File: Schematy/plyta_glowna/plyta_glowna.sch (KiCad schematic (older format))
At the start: 6 parts

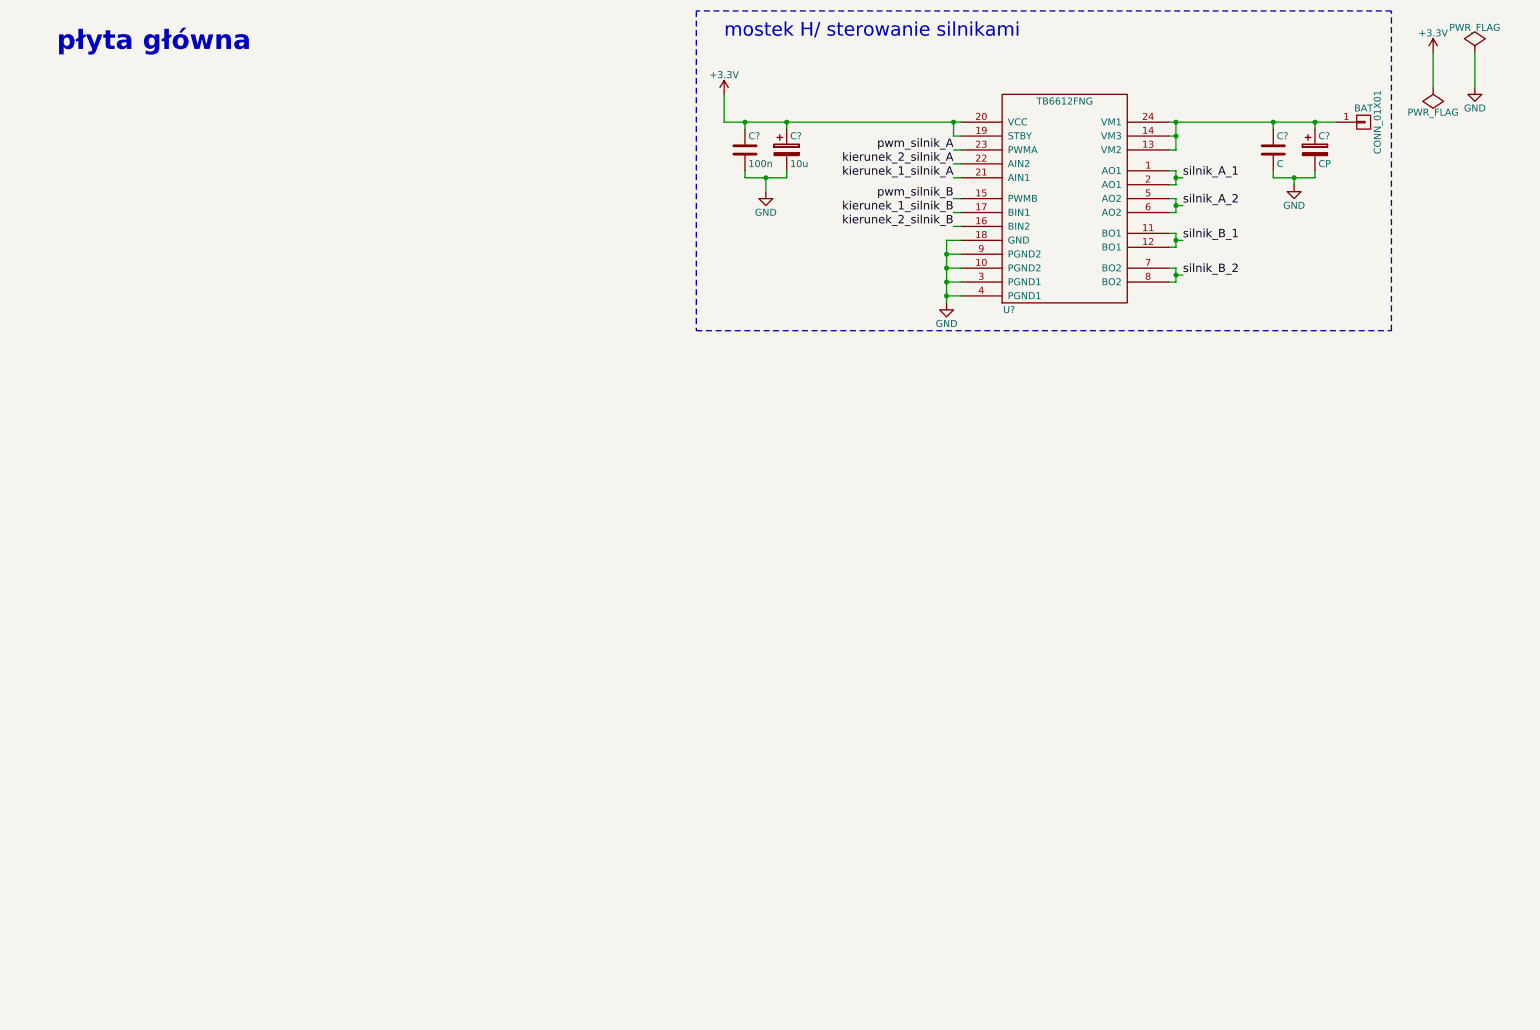
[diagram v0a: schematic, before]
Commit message: Płyta główna + listwa [do sprawdzenia]
do zrobienia:
- układ pomiarowy napięcia na akumulatorze
- wskaźnik naładowania akumulatora na 3 led
- dobrać złącza
- zagospodarować pozostałe piny
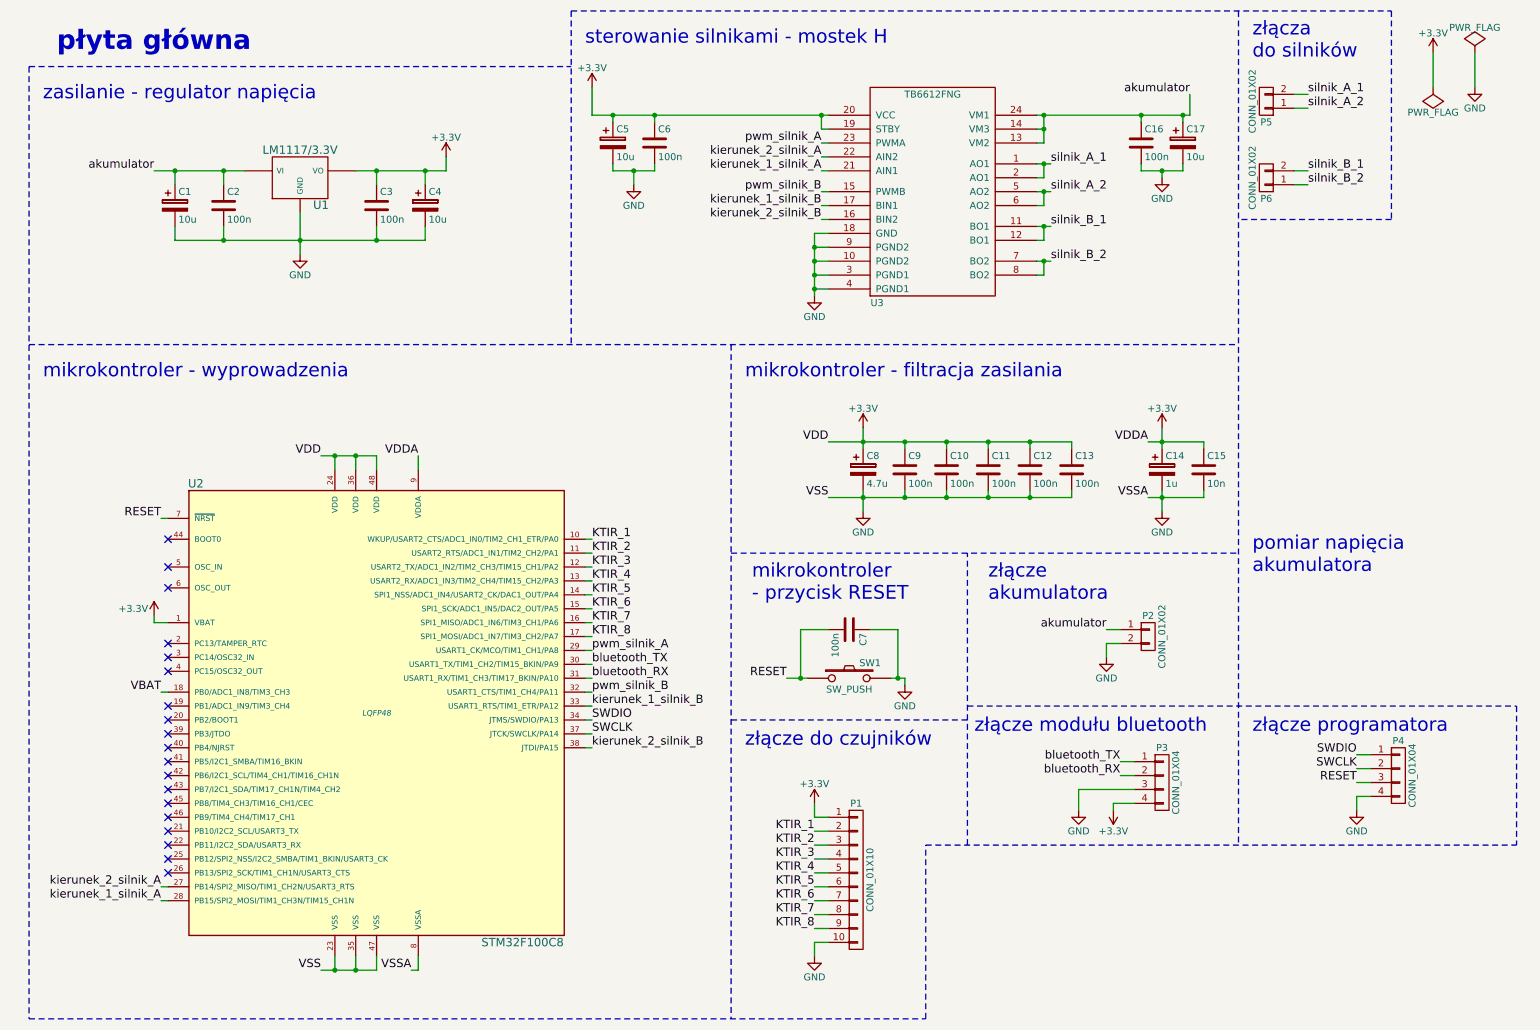
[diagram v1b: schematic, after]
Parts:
- removed BAT: CONN_01X01, symbol CONN_01X01
- added C1, C4: 10u, symbol CP
- added C10, C11, C12, C13, C2, C3, C7, C9: 100n, symbol C
- added C14: 1u, symbol CP
- added C15: 10n, symbol C
- added C8: 4.7u, symbol CP
- added P1: CONN_01X10, symbol CONN_01X10
- added P2, P5, P6: CONN_01X02, symbol CONN_01X02
- added P3, P4: CONN_01X04, symbol CONN_01X04
- added SW1: SW_PUSH, symbol SW_PUSH
- added U1: LM1117/3.3V, symbol LM1117
- added U2: STM32F100C8, LQFP48, symbol STM32F100C8
- C16: renamed from C?; value C -> 100n
- C17: renamed from C?; value CP -> 10u
- gave numbers to parts that had none: 3
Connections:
- net +3V3: now also C10.1, C11.1, C12.1, C13.1, C14.1, C15.1, C3.1, C4.1, C8.1, C9.1, P1.1 (P1), P3.4 (P4), U1.2 (VO), U2.1 (VBAT), U2.24 (VDD), U2.36 (VDD), U2.48 (VDD), U2.9 (VDDA)
- net GND: now also C1.2, C10.2, C11.2, C12.2, C13.2, C14.2, C15.2, C2.2, C3.2, C4.2, C7.1, C8.2, C9.2, P1.10 (P10), P2.2 (P2), P3.3 (P3), P4.4 (P4), SW1.2, U1.3 (GND), U2.23 (VSS), U2.35 (VSS), U2.47 (VSS), U2.8 (VSSA)
- net kierunek_1_silnik_A: now also U2.28 (PB15/SPI2_MOSI/TIM1_CH3N/TIM15_CH1N)
- net kierunek_1_silnik_B: now also U2.33 (USART1_RTS/TIM1_ETR/PA12)
- net kierunek_2_silnik_A: now also U2.27 (PB14/SPI2_MISO/TIM1_CH2N/USART3_RTS)
- net kierunek_2_silnik_B: now also U2.38 (JTDI/PA15)
- net pwm_silnik_A: now also U2.29 (USART1_CK/MCO/TIM1_CH1/PA8)
- net pwm_silnik_B: now also U2.32 (USART1_CTS/TIM1_CH4/PA11)
- net silnik_A_1: now also P5.2 (P2)
- net silnik_A_2: now also P5.1 (P1)
- net silnik_B_1: now also P6.2 (P2)
- net silnik_B_2: now also P6.1 (P1)
- net akumulator: now reaches C16.1, C17.1, U3.13 (VM2), U3.14 (VM3), U3.24 (VM1)
- net akumulator: now also C1.1, C2.1, P2.1 (P1), U1.1 (VI)
- new net KTIR_1: P1.2 (P2), U2.10 (WKUP/USART2_CTS/ADC1_IN0/TIM2_CH1_ETR/PA0)
- new net KTIR_2: P1.3 (P3), U2.11 (USART2_RTS/ADC1_IN1/TIM2_CH2/PA1)
- new net KTIR_3: P1.4 (P4), U2.12 (USART2_TX/ADC1_IN2/TIM2_CH3/TIM15_CH1/PA2)
- new net KTIR_4: P1.5 (P5), U2.13 (USART2_RX/ADC1_IN3/TIM2_CH4/TIM15_CH2/PA3)
- new net KTIR_5: P1.6 (P6), U2.14 (SPI1_NSS/ADC1_IN4/USART2_CK/DAC1_OUT/PA4)
- new net KTIR_6: P1.7 (P7), U2.15 (SPI1_SCK/ADC1_IN5/DAC2_OUT/PA5)
- new net KTIR_7: P1.8 (P8), U2.16 (SPI1_MISO/ADC1_IN6/TIM3_CH1/PA6)
- new net KTIR_8: P1.9 (P9), U2.17 (SPI1_MOSI/ADC1_IN7/TIM3_CH2/PA7)
- new net RESET: C7.2, P4.3 (P3), SW1.1, U2.7 (~NRST)
- new net SWCLK: P4.2 (P2), U2.37 (JTCK/SWCLK/PA14)
- new net SWDIO: P4.1 (P1), U2.34 (JTMS/SWDIO/PA13)
- new net VBAT: U2.18 (PB0/ADC1_IN8/TIM3_CH3)
- new net bluetooth_RX: P3.2 (P2), U2.31 (USART1_RX/TIM1_CH3/TIM17_BKIN/PA10)
- new net bluetooth_TX: P3.1 (P1), U2.30 (USART1_TX/TIM1_CH2/TIM15_BKIN/PA9)
- no-connect marks 0 -> 19
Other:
- note added: "mikrokontroler - filtracja zasilania"
- note added: "mikrokontroler - wyprowadzenia"
- note added: "mikrokontroler\n- przycisk RESET"
- note added: "pomiar napięcia\nakumulatora"
- note added: "sterowanie silnikami - mostek H"
- note added: "zasilanie - regulator napięcia"
- note added: "złącza\ndo silników"
- note added: "złącze do czujników"
- note added: "złącze modułu bluetooth"
- note added: "złącze programatora"
- note added: "złącze\nakumulatora"
- note removed: "mostek H/ sterowanie silnikami"
- moved on the sheet: C16, C17, C5, C6, U3

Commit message: Kompletny schemat elektryczny [do sprawdzenia]
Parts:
- removed P3, P4: CONN_01X04, symbol CONN_01X04
- added C18, C19: 100n, symbol C
- added D1, D10, D11, D12, D13, D14, D2, D3, D4, D5, D6, D7, D8, D9: LED, symbol LED
- added P3: CONN_01X06, symbol CONN_01X06
- added P4: CONN_01X05, symbol CONN_01X05
- added R1, R10, R11, R14, R15, R16, R2, R3, R4, R5, R6, R7, R8, R9: 100, symbol R
- added R12: 22K, symbol R
- added R13: 10K, symbol R
- added SW2, SW3: start/stop, symbol SW_PUSH
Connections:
- net +3V3: now also D12.2 (A), P3.2 (P2), P4.1 (P1)
- net GND: now also C18.1, C19.1, P3.1 (P1), P4.5 (P5), R1.1, R10.1, R11.1, R13.2, R14.2, R15.1, R16.1, R2.1, R3.1, R4.1, R5.1, R6.1, R7.1, R8.1, R9.1, SW2.2, SW3.2
- net RESET: now also P4.4 (P4)
- net SWCLK: now also P4.3 (P3)
- net SWDIO: now also P4.2 (P2)
- net akumulator: now also R12.1
- net bluetooth_RX: now also U2.43 (PB7/I2C1_SDA/TIM17_CH1N/TIM4_CH2), P3.5 (P5); no longer U2.31 (USART1_RX/TIM1_CH3/TIM17_BKIN/PA10)
- net bluetooth_TX: now also U2.42 (PB6/I2C1_SCL/TIM4_CH1/TIM16_CH1N), P3.4 (P4); no longer U2.30 (USART1_TX/TIM1_CH2/TIM15_BKIN/PA9)
- net kierunek_1_silnik_A: now also U2.26 (PB13/SPI2_SCK/TIM1_CH1N/USART3_CTS); no longer U2.28 (PB15/SPI2_MOSI/TIM1_CH3N/TIM15_CH1N)
- net kierunek_1_silnik_B: now also U2.27 (PB14/SPI2_MISO/TIM1_CH2N/USART3_RTS); no longer U2.33 (USART1_RTS/TIM1_ETR/PA12)
- net kierunek_2_silnik_A: now also U2.25 (PB12/SPI2_NSS/I2C2_SMBA/TIM1_BKIN/USART3_CK); no longer U2.27 (PB14/SPI2_MISO/TIM1_CH2N/USART3_RTS)
- net kierunek_2_silnik_B: now also U2.28 (PB15/SPI2_MOSI/TIM1_CH3N/TIM15_CH1N); no longer U2.38 (JTDI/PA15)
- net pwm_silnik_B: now also U2.30 (USART1_TX/TIM1_CH2/TIM15_BKIN/PA9); no longer U2.32 (USART1_CTS/TIM1_CH4/PA11)
- net led_wsk_nal_1: now reaches U2.19 (PB1/ADC1_IN9/TIM3_CH4)
- net led_wsk_nal_1: now also D9.2 (A)
- net led_ktir_5: now reaches U2.2 (PC13/TAMPER_RTC)
- net led_ktir_5: now also D5.2 (A)
- net led_wsk_nal_2: now reaches U2.20 (PB2/BOOT1)
- net led_wsk_nal_2: now also D10.2 (A)
- net led_wsk_nal_3: now reaches U2.21 (PB10/I2C2_SCL/USART3_TX)
- net led_wsk_nal_3: now also D11.2 (A)
- net led_ktir_4: now reaches U2.3 (PC14/OSC32_IN)
- net led_ktir_4: now also D4.2 (A)
- net led_ktir_8: now reaches U2.39 (PB3/JTDO)
- net led_ktir_8: now also D8.2 (A)
- net led_ktir_3: now reaches U2.4 (PC15/OSC32_OUT)
- net led_ktir_3: now also D3.2 (A)
- net led_ktir_7: now reaches U2.40 (PB4/NJRST)
- net led_ktir_7: now also D7.2 (A)
- net led_ktir_6: now reaches U2.41 (PB5/I2C1_SMBA/TIM16_BKIN)
- net led_ktir_6: now also D6.2 (A)
- net bluetooth_key: now reaches U2.45 (PB8/TIM4_CH3/TIM16_CH1/CEC)
- net bluetooth_key: now also P3.6 (P6)
- net start/stop: now reaches U2.46 (PB9/TIM4_CH4/TIM17_CH1)
- net start/stop: now also C18.2, SW2.1
- net led_ktir_2: now reaches U2.5 (OSC_IN)
- net led_ktir_2: now also D2.2 (A)
- net led_ktir_1: now reaches U2.6 (OSC_OUT)
- net led_ktir_1: now also D1.2 (A)
- net VBAT renamed Vaku
- net Vaku: now also R12.2, R13.1
- net silnik_A_1: no longer names the net of U3.1 (AO1), U3.2 (AO1)
- net silnik_A_1: now also P5.1 (P1); no longer P5.2 (P2)
- net silnik_A_2: no longer names the net of U3.5 (AO2), U3.6 (AO2)
- net silnik_A_2: now also P5.2 (P2); no longer P5.1 (P1)
- net silnik_B_1: no longer names the net of U3.11 (BO1), U3.12 (BO1)
- net silnik_B_1: now also P6.1 (P1); no longer P6.2 (P2)
- net silnik_B_2: no longer names the net of U3.7 (BO2), U3.8 (BO2)
- net silnik_B_2: now also P6.2 (P2); no longer P6.1 (P1)
- new net: D9.1 (K), R9.2
- new net: D10.1 (K), R10.2
- new net: D11.1 (K), R11.2
- new net: D12.1 (K), R14.1
- new net: D13.1 (K), R15.2
- new net: D14.1 (K), R16.2
- new net: D1.1 (K), R1.2
- new net: D2.1 (K), R2.2
- new net: D3.1 (K), R3.2
- new net: D4.1 (K), R4.2
- new net: D5.1 (K), R5.2
- new net: D6.1 (K), R6.2
- new net: D7.1 (K), R7.2
- new net: D8.1 (K), R8.2
- new net led_debug_1: D13.2 (A), U2.31 (USART1_RX/TIM1_CH3/TIM17_BKIN/PA10)
- new net led_debug_2: D14.2 (A), U2.32 (USART1_CTS/TIM1_CH4/PA11)
- new net przycisk_debug: C19.2, SW3.1, U2.33 (USART1_RTS/TIM1_ETR/PA12)
- no-connect marks 19 -> 4
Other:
- note added: "ledy do debugowania"
- note added: "ledy odwzorowujące stany czujników"
- note added: "przycisk do debugowania"
- note added: "przycisk start/ stop"
- note added: "sterownik silników"
- note added: "wskaźnik naładowania \nakumulatora"
- note added: "złącze modułu \nbluetooth"
- note removed: "płyta główna"
- note removed: "sterowanie silnikami - mostek H"
- note removed: "złącza\ndo silników"
- note removed: "złącze modułu bluetooth"
- moved on the sheet: C1, C10, C11, C12, C13, C14, C15, C16, C17, C2, C3, C4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

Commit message: Schemat elektryczny
@edit
zmiana modułu bluetooth z HC-05 na HC-06
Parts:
- removed P3: CONN_01X06, symbol CONN_01X06
- added P?: CONN_01X04, symbol CONN_01X04
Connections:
- net +3V3: now also P?.4 (P4)
- net GND: now also P?.3 (P3)
- net bluetooth_RX: now also P?.1 (P1)
- net bluetooth_TX: now also P?.2 (P2)
- net bluetooth_key: no longer names the net of U2.45 (PB8/TIM4_CH3/TIM16_CH1/CEC)
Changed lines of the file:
@@
 encoding utf-8
 Sheet 1 1
-Title "Robot - płyta główna"
+Title "projekT-3 - płyta główna"
 Date "2016-11-03"
-Rev "Piotr Bielenia"
+Rev ""
 Comp ""
-Comment1 ""
+Comment1 "Piotr Bielenia, Andrzej Gołębiewski"
 Comment2 ""
 Comment3 ""
@@
 Text Label 4450 5950 2    60   ~ 0
 kierunek_1_silnik_B
-Text Label 5950 7950 2    60   ~ 0
+Text Label 5950 7750 2    60   ~ 0
 bluetooth_TX
-Text Label 5950 8050 2    60   ~ 0
+Text Label 5950 7650 2    60   ~ 0
 bluetooth_RX
 $Comp
 L GND #PWR015
 U 1 1 581B444B
-P 6050 7400
-F 0 "#PWR015" H 6050 7150 50  0001 C CNN
-F 1 "GND" H 6150 7400 50  0000 C CNN
-F 2 "" H 6050 7400 50  0000 C CNN
-F 3 "" H 6050 7400 50  0000 C CNN
-	1    6050 7400
+P 5850 7900
+F 0 "#PWR015" H 5850 7650 50  0001 C CNN
+F 1 "GND" H 5750 7750 50  0000 C CNN
+F 2 "" H 5850 7900 50  0000 C CNN
+F 3 "" H 5850 7900 50  0000 C CNN
+	1    5850 7900
 	1    0    0    -1
 $EndComp
@@
 L +3.3V #PWR018
 U 1 1 581B779C
-P 5900 7750
-F 0 "#PWR018" H 5900 7600 50  0001 C CNN
-F 1 "+3.3V" H 6050 7800 50  0000 C CNN
-F 2 "" H 5900 7750 50  0000 C CNN
-F 3 "" H 5900 7750 50  0000 C CNN
-	1    5900 7750
+P 5950 8050
+F 0 "#PWR018" H 5950 7900 50  0001 C CNN
+F 1 "+3.3V" H 5850 8200 50  0000 C CNN
+F 2 "" H 5950 8050 50  0000 C CNN
+F 3 "" H 5950 8050 50  0000 C CNN
+	1    5950 8050
 	-1   0    0    1
 $EndComp
@@
 	2850 1600 2850 1850
 Connection ~ 3200 1850
-$Comp
-L CONN_01X06 P3
-U 1 1 581F01A8
-P 6200 7900
-F 0 "P3" H 6200 8250 50  0000 C CNN
-F 1 "CONN_01X06" V 6300 7900 50  0000 C CNN
-F 2 "" H 6200 7900 50  0000 C CNN
-F 3 "" H 6200 7900 50  0000 C CNN
-	1    6200 7900
-	1    0    0    -1
-$EndComp
-Wire Wire Line
-	6050 7350 6050 7400
-Wire Wire Line
-	5900 7350 6050 7350
-Wire Wire Line
-	5900 7350 5900 7650
-Wire Wire Line
-	5900 7650 6000 7650
-NoConn ~ 6000 7850
-Wire Wire Line
-	6000 7750 5900 7750
-Wire Wire Line
-	5950 7950 6000 7950
-Wire Wire Line
-	5950 8050 6000 8050
-Text Label 5950 8150 2    60   ~ 0
-bluetooth_key
-Wire Wire Line
-	5950 8150 6000 8150
-Text Label 4450 5350 2    60   ~ 0
-bluetooth_key
-Wire Wire Line
-	4450 5350 4500 5350
 $Comp
 L SW_PUSH SW2
@@
 Wire Notes Line
 	8400 3750 8400 5400
+$Comp
+L CONN_01X04 P?
+U 1 1 581D0D24
+P 6200 7800
+F 0 "P?" H 6200 8050 50  0000 C CNN
+F 1 "CONN_01X04" V 6300 7800 50  0000 C CNN
+F 2 "" H 6200 7800 50  0000 C CNN
+F 3 "" H 6200 7800 50  0000 C CNN
+	1    6200 7800
+	1    0    0    -1
+$EndComp
+Wire Wire Line
+	5950 8050 5950 7950
+Wire Wire Line
+	5950 7950 6000 7950
+Wire Wire Line
+	5850 7900 5850 7850
+Wire Wire Line
+	5850 7850 6000 7850
+Wire Wire Line
+	5950 7650 6000 7650
+Wire Wire Line
+	6000 7750 5950 7750
+NoConn ~ 4500 5350
 $EndSCHEMATC
